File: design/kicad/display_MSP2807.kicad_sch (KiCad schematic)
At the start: 3 parts

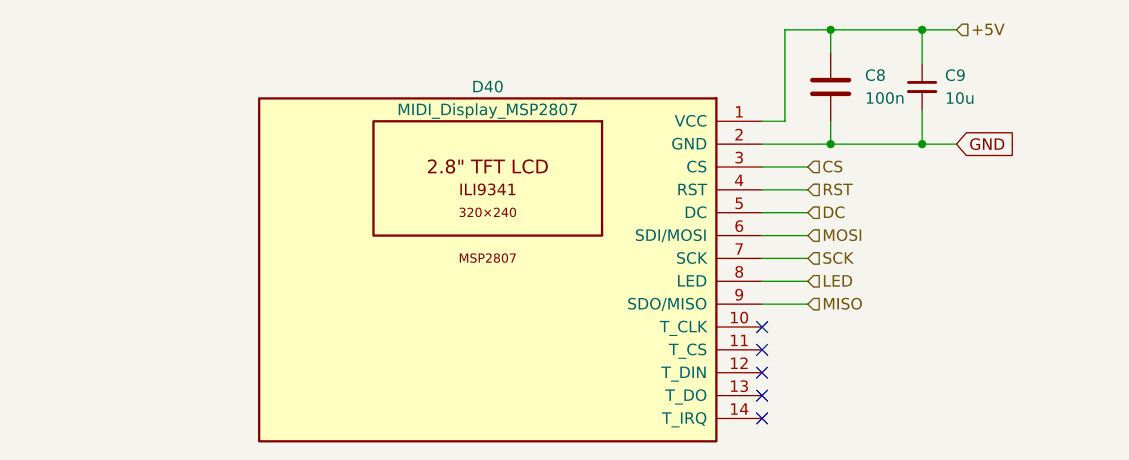
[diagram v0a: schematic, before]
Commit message: Fix reference labels and update wire connections in MIDI controller and multiplexer schematics
- Adjusted wire connection points in the MIDI controller schematic for better alignment.
- Updated label positions for various components in the MIDI controller schematic.
- Renamed reference designators for capacitors and power connections in the multiplexer schematic to maintain consistency.
- Corrected the reference designators for multiple components to reflect accurate labeling.
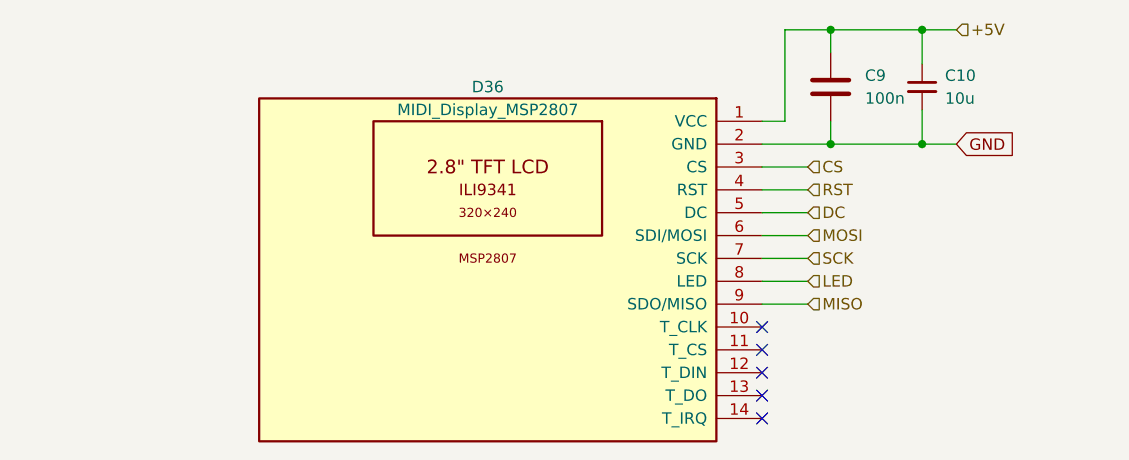
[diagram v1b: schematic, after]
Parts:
- renumbered C9 to C10, C8 to C9, D40 to D36
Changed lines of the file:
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@@
 		(dnp no)
 		(fields_autoplaced yes)
-		(property "Reference" "C9"
+		(property "Reference" "C10"
 			(at 172.72 67.3162 0)
 			(effects
@@
 			(project ""
 				(path "/9e44e663-00d0-4f33-bf1f-c4ad78deb554/b074c366-2f0b-4fcc-8b9f-7590ca8943b4"
-					(reference "C9")
+					(reference "C10")
 					(unit 1)
 				)
@@
 		(on_board yes)
 		(dnp no)
-		(property "Reference" "D40"
+		(property "Reference" "D36"
 			(at 121.92 68.58 0)
 			(effects
@@
 			(project "midi_controller"
 				(path "/9e44e663-00d0-4f33-bf1f-c4ad78deb554/b074c366-2f0b-4fcc-8b9f-7590ca8943b4"
-					(reference "D40")
+					(reference "D36")
 					(unit 1)
 				)
@@
 		(dnp no)
 		(fields_autoplaced yes)
-		(property "Reference" "C8"
+		(property "Reference" "C9"
 			(at 163.83 67.3099 0)
 			(effects
@@
 			(project "midi_controller"
 				(path "/9e44e663-00d0-4f33-bf1f-c4ad78deb554/b074c366-2f0b-4fcc-8b9f-7590ca8943b4"
-					(reference "C8")
+					(reference "C9")
 					(unit 1)
 				)

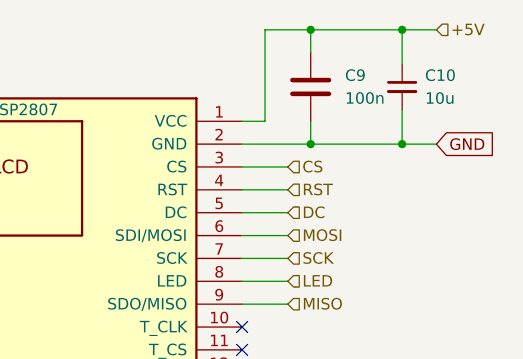
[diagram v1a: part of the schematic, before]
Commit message: Update capacitor references in multiplexer schematic
Changed capacitor references from C11 to C42 and C12 to C43 in the multiplexer_CD74HC4067M schematic. Updated instances accordingly to maintain consistency in the design.
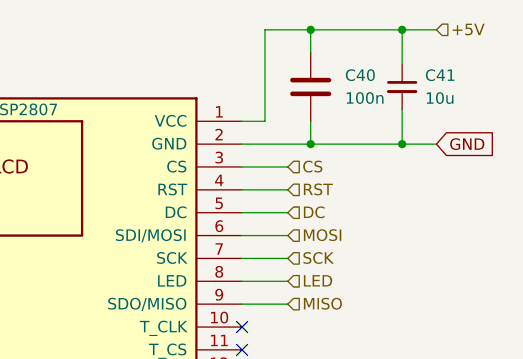
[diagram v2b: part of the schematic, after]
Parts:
- renumbered C9 to C40, C10 to C41
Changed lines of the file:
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@@
 		(dnp no)
 		(fields_autoplaced yes)
-		(property "Reference" "C10"
+		(property "Reference" "C41"
 			(at 172.72 67.3162 0)
 			(effects
@@
 			(project ""
 				(path "/9e44e663-00d0-4f33-bf1f-c4ad78deb554/b074c366-2f0b-4fcc-8b9f-7590ca8943b4"
-					(reference "C10")
+					(reference "C41")
 					(unit 1)
 				)
@@
 		(dnp no)
 		(fields_autoplaced yes)
-		(property "Reference" "C9"
+		(property "Reference" "C40"
 			(at 163.83 67.3099 0)
 			(effects
@@
 			(project "midi_controller"
 				(path "/9e44e663-00d0-4f33-bf1f-c4ad78deb554/b074c366-2f0b-4fcc-8b9f-7590ca8943b4"
-					(reference "C9")
+					(reference "C40")
 					(unit 1)
 				)

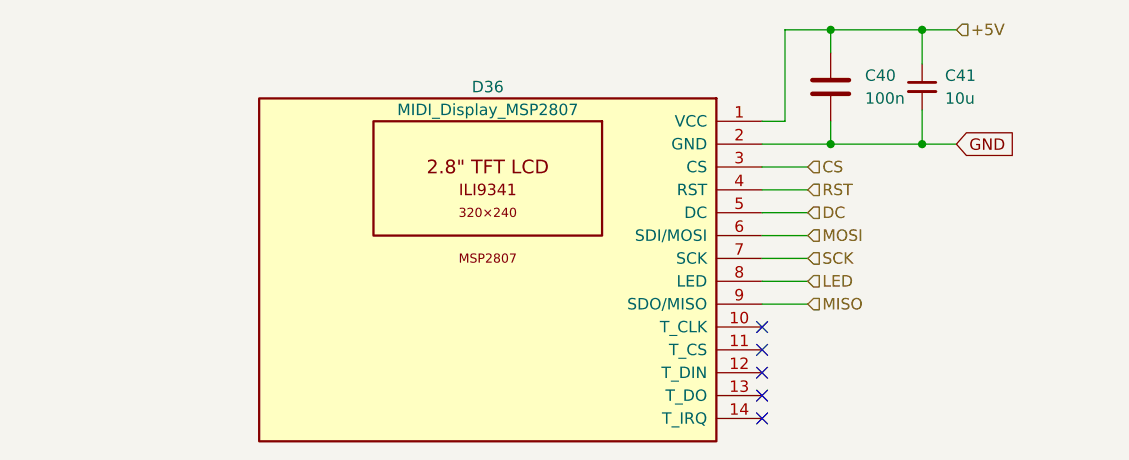
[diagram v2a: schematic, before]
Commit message: Update kicad binary files
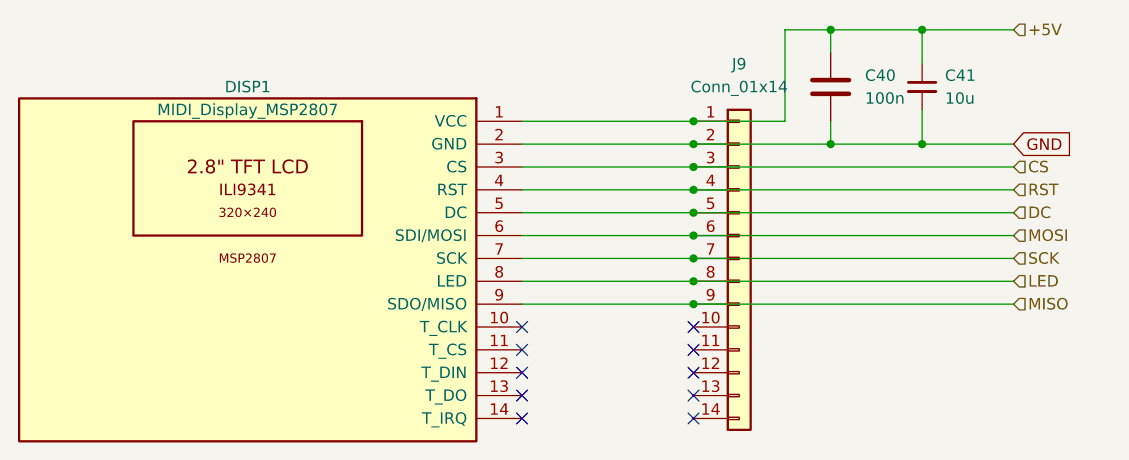
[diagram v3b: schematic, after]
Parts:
- added J9: Conn_01x14, Connector_PinSocket_2.54mm:PinSocket_1x14_P2.54mm_Vertical, symbol Connector_Generic:Conn_01x14
- renumbered D36 to DISP1
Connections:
- net +5V: now also J9.1 (Pin_1)
- net CS: now also J9.3 (Pin_3)
- net DC: now also J9.5 (Pin_5)
- net GND: now also J9.2 (Pin_2)
- net LED: now also J9.8 (Pin_8)
- net MISO: now also J9.9 (Pin_9)
- net MOSI: now also J9.6 (Pin_6)
- net RST: now also J9.4 (Pin_4)
- net SCK: now also J9.7 (Pin_7)
- no-connect marks 5 -> 10
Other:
- moved on the sheet: DISP1

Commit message: Update kicad binary files
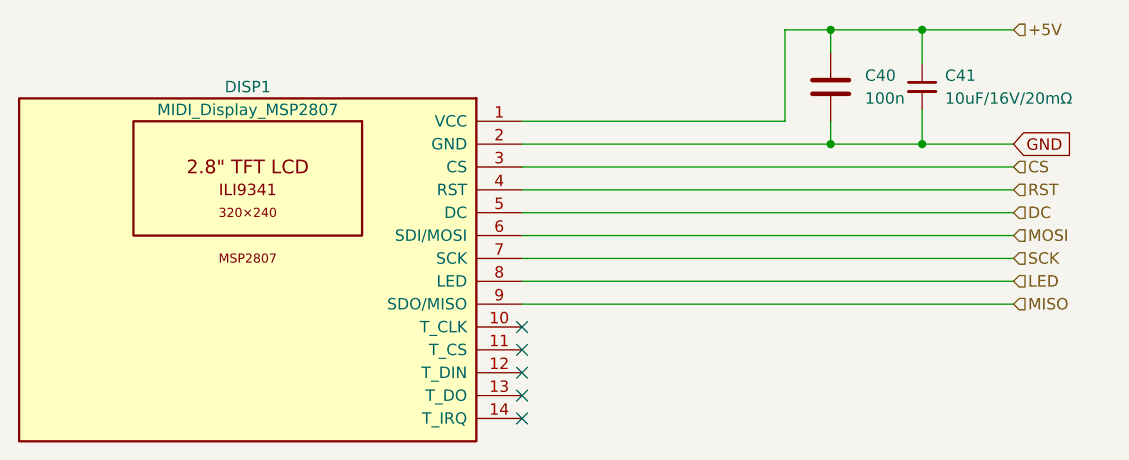
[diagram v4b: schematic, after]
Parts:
- removed J9: Conn_01x14, Connector_PinSocket_2.54mm:PinSocket_1x14_P2.54mm_Vertical, symbol Connector_Generic:Conn_01x14
- C41: footprint Capacitor_SMD:C_0805_2012Metric -> 4ms_Capacitor:C_0805; Display 10u -> 10uF/16V/20mΩ
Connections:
- no-connect marks 10 -> 5

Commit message: Update kicad binary files
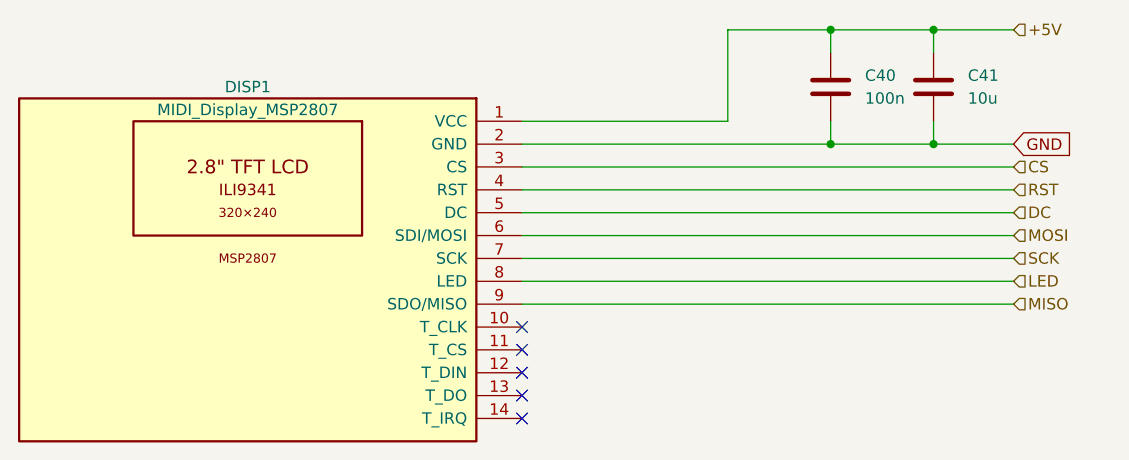
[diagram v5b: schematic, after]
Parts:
- C41: value 10uF_0805_16V_lowESR -> 10u; footprint 4ms_Capacitor:C_0805 -> Capacitor_SMD:C_0805_2012Metric; symbol PCM_4ms_Capacitor:10uF_0805_16V_lowESR -> Device:C; Display 10uF/16V/20mΩ -> (none); JLCPCB ID C190442 -> (none); Manufacturer Taiyo Yuden -> (none); Part Number EMK212ABJ106KG-T -> (none); Specifications 10uF, Min. 16V, ESR<=20mΩ@1MHz, 0805, MLCC -> (none)
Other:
- moved on the sheet: C41
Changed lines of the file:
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@@
 	(paper "A4")
+	(junction
+		(at 171.45 62.23)
+		(diameter 0)
+		(color 0 0 0 0)
+	)
 	(junction
 		(at 160.02 62.23)
@@
 	)
 	(junction
-		(at 170.18 62.23)
-		(diameter 0)
-		(color 0 0 0 0)
-	)
-	(junction
-		(at 170.18 74.93)
+		(at 171.45 74.93)
 		(diameter 0)
 		(color 0 0 0 0)
@@
 	(wire
 		(pts
-			(xy 160.02 74.93) (xy 170.18 74.93)
+			(xy 160.02 74.93) (xy 171.45 74.93)
+		)
+		(stroke
+			(width 0)
+			(type default)
+		)
+	)
+	(wire
+		(pts
+			(xy 171.45 62.23) (xy 180.34 62.23)
 		)
 		(stroke
@@
 	(wire
 		(pts
-			(xy 160.02 62.23) (xy 170.18 62.23)
-		)
-		(stroke
-			(width 0)
-			(type default)
-		)
-	)
-	(wire
-		(pts
 			(xy 125.73 82.55) (xy 180.34 82.55)
 		)
@@
 	(wire
 		(pts
+			(xy 171.45 74.93) (xy 180.34 74.93)
+		)
+		(stroke
+			(width 0)
+			(type default)
+		)
+	)
+	(wire
+		(pts
 			(xy 125.73 92.71) (xy 180.34 92.71)
 		)
@@
 	(wire
 		(pts
-			(xy 125.73 72.39) (xy 154.94 72.39)
-		)
-		(stroke
-			(width 0)
-			(type default)
-		)
-	)
-	(wire
-		(pts
-			(xy 170.18 62.23) (xy 170.18 66.04)
+			(xy 125.73 72.39) (xy 148.59 72.39)
 		)
 		(stroke
@@
 	(wire
 		(pts
-			(xy 170.18 74.93) (xy 180.34 74.93)
-		)
-		(stroke
-			(width 0)
-			(type default)
-		)
-	)
-	(wire
-		(pts
 			(xy 125.73 80.01) (xy 180.34 80.01)
 		)
@@
 	(wire
 		(pts
+			(xy 171.45 62.23) (xy 171.45 64.77)
+		)
+		(stroke
+			(width 0)
+			(type default)
+		)
+	)
+	(wire
+		(pts
 			(xy 160.02 72.39) (xy 160.02 74.93)
 		)
@@
 	(wire
 		(pts
-			(xy 170.18 62.23) (xy 180.34 62.23)
+			(xy 160.02 62.23) (xy 171.45 62.23)
 		)
 		(stroke
@@
 	(wire
 		(pts
-			(xy 154.94 62.23) (xy 160.02 62.23)
-		)
-		(stroke
-			(width 0)
-			(type default)
-		)
-	)
-	(wire
-		(pts
-			(xy 154.94 62.23) (xy 154.94 72.39)
-		)
-		(stroke
-			(width 0)
-			(type default)
-		)
-	)
-	(wire
-		(pts
-			(xy 170.18 71.12) (xy 170.18 74.93)
+			(xy 148.59 62.23) (xy 160.02 62.23)
+		)
+		(stroke
+			(width 0)
+			(type default)
+		)
+	)
+	(wire
+		(pts
+			(xy 171.45 72.39) (xy 171.45 74.93)
+		)
+		(stroke
+			(width 0)
+			(type default)
+		)
+	)
+	(wire
+		(pts
+			(xy 148.59 62.23) (xy 148.59 72.39)
 		)
 		(stroke
@@
 	)
 	(symbol
-		(lib_id "PCM_4ms_Capacitor:10uF_0805_16V_lowESR")
-		(at 170.18 68.58 0)
+		(lib_id "Device:C")
+		(at 171.45 68.58 0)
 		(unit 1)
 		(exclude_from_sim no)
@@
 		(fields_autoplaced yes)
 		(property "Reference" "C41"
-			(at 172.72 67.3162 0)
+			(at 175.26 67.3099 0)
 			(effects
 				(font
@@
 			)
 		)
-		(property "Value" "10uF_0805_16V_lowESR"
-			(at 170.18 64.77 0)
+		(property "Value" "10u"
+			(at 175.26 69.8499 0)
+			(effects
+				(font
+					(size 1.27 1.27)
+				)
+				(justify left)
+			)
+		)
+		(property "Footprint" "Capacitor_SMD:C_0805_2012Metric"
+			(at 172.4152 72.39 0)
 			(effects
 				(font
@@
 			)
 		)
-		(property "Footprint" "4ms_Capacitor:C_0805"
-			(at 167.64 73.66 0)
-			(effects
-				(font
-					(size 1.27 1.27)
-				)
-				(justify left)
+		(property "Datasheet" "~"
+			(at 171.45 68.58 0)
+			(effects
+				(font
+					(size 1.27 1.27)
+				)
 				(hide yes)
 			)
 		)
-		(property "Datasheet" ""
-			(at 170.18 68.58 0)
-			(effects
-				(font
-					(size 1.27 1.27)
-				)
-				(hide yes)
-			)
-		)
-		(property "Description" "10uF, Min. 16V, ESR<=20mΩ@1MHz, 0805, MLCC"
-			(at 170.18 68.58 0)
-			(effects
-				(font
-					(size 1.27 1.27)
-				)
-				(hide yes)
-			)
-		)
-		(property "Specifications" "10uF, Min. 16V, ESR<=20mΩ@1MHz, 0805, MLCC"
-			(at 167.64 76.454 0)
-			(effects
-				(font
-					(size 1.27 1.27)
-				)
-				(justify left)
-				(hide yes)
-			)
-		)
-		(property "Manufacturer" "Taiyo Yuden"
-			(at 167.64 77.978 0)
-			(effects
-				(font
-					(size 1.27 1.27)
-				)
-				(justify left)
-				(hide yes)
-			)
-		)
-		(property "Part Number" "EMK212ABJ106KG-T"
-			(at 167.64 79.502 0)
-			(effects
-				(font
-					(size 1.27 1.27)
-				)
-				(justify left)
-				(hide yes)
-			)
-		)
-		(property "Display" "10uF/16V/20mΩ"
-			(at 172.72 69.8562 0)
-			(effects
-				(font
-					(size 1.27 1.27)
-				)
-				(justify left)
-			)
-		)
-		(property "JLCPCB ID" "C190442"
-			(at 170.18 68.58 0)
-			(effects
-				(font
+		(property "Description" "Unpolarized capacitor"
+			(at 171.45 68.58 0)
+			(effects
+				(font

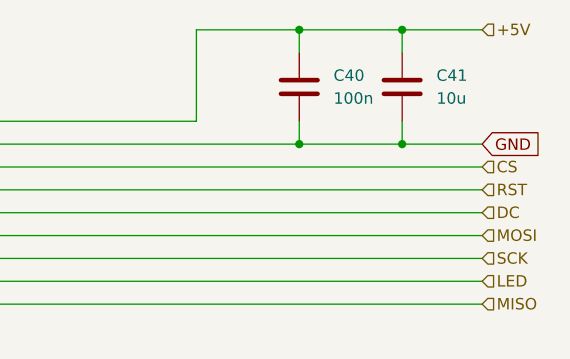
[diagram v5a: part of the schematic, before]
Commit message: Update kicad binary files
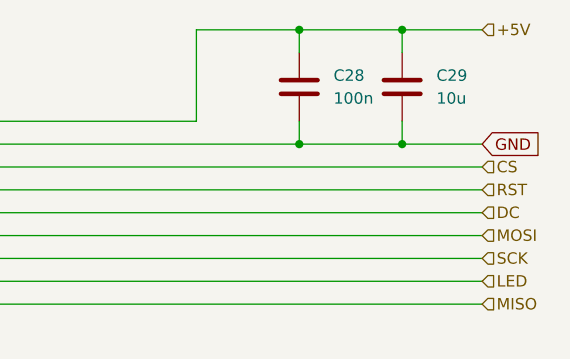
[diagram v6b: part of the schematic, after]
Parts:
- C28: renamed from C40; LCSC (none) -> C1711
- C29: renamed from C41; Display (none) -> 10u; JLCPCB ID (none) -> C1713; LCSC (none) -> C1713; Manufacturer (none) -> Taiyo Yuden; Part Number (none) -> EMK212ABJ106KG-T; Specifications (none) -> 10uF, Min. 16V, ESR<=20mΩ@1MHz, 0805, MLCC
- DISP1: now left out of the parts list
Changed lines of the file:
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@@
 		(dnp no)
 		(fields_autoplaced yes)
-		(property "Reference" "C41"
+		(property "Reference" "C29"
 			(at 175.26 67.3099 0)
 			(effects
@@
 		)
 		(property "Description" "Unpolarized capacitor"
+			(at 171.45 68.58 0)
+			(effects
+				(font
+					(size 1.27 1.27)
+				)
+				(hide yes)
+			)
+		)
+		(property "LCSC" "C1713"
+			(at 175.26 67.3099 0)
+			(effects
+				(font
+					(size 1.27 1.27)
+				)
+				(hide yes)
+			)
+		)
+		(property "Display" "10u"
+			(at 171.45 68.58 0)
+			(effects
+				(font
+					(size 1.27 1.27)
+				)
+				(hide yes)
+			)
+		)
+		(property "JLCPCB ID" "C1713"
+			(at 171.45 68.58 0)
+			(effects
+				(font
+					(size 1.27 1.27)
+				)
+				(hide yes)
+			)
+		)
+		(property "Manufacturer" "Taiyo Yuden"
+			(at 171.45 68.58 0)
+			(effects
+				(font
+					(size 1.27 1.27)
+				)
+				(hide yes)
+			)
+		)
+		(property "Part Number" "EMK212ABJ106KG-T"
+			(at 171.45 68.58 0)
+			(effects
+				(font
+					(size 1.27 1.27)
+				)
+				(hide yes)
+			)
+		)
+		(property "Specifications" "10uF, Min. 16V, ESR<=20mΩ@1MHz, 0805, MLCC"
 			(at 171.45 68.58 0)
 			(effects
@@
 			(project ""
 				(path "/9e44e663-00d0-4f33-bf1f-c4ad78deb554/b074c366-2f0b-4fcc-8b9f-7590ca8943b4"
-					(reference "C41")
+					(reference "C29")
 					(unit 1)
 				)
@@
 		(unit 1)
 		(exclude_from_sim no)
-		(in_bom yes)
+		(in_bom no)
 		(on_board yes)
 		(dnp no)
@@
 		(dnp no)
 		(fields_autoplaced yes)
-		(property "Reference" "C40"
+		(property "Reference" "C28"
 			(at 163.83 67.3099 0)
 			(effects
@@
 		(property "Description" "Unpolarized capacitor"
 			(at 160.02 68.58 0)
+			(effects
+				(font
+					(size 1.27 1.27)
+				)
+				(hide yes)
+			)
+		)
+		(property "LCSC" "C1711"
+			(at 163.83 67.3099 0)
 			(effects
 				(font
@@
 			(project "midi_controller"
 				(path "/9e44e663-00d0-4f33-bf1f-c4ad78deb554/b074c366-2f0b-4fcc-8b9f-7590ca8943b4"
-					(reference "C40")
+					(reference "C28")
 					(unit 1)
 				)

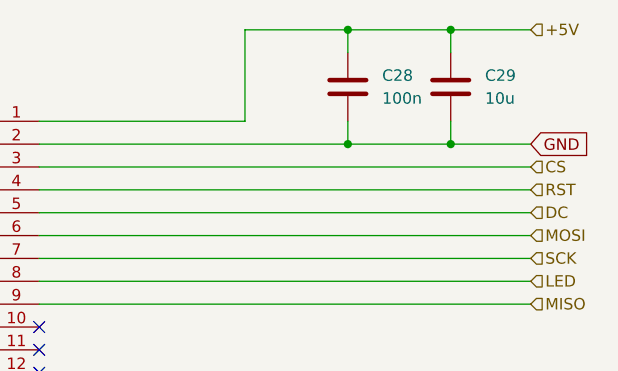
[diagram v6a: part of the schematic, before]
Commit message: Update kicad binary files
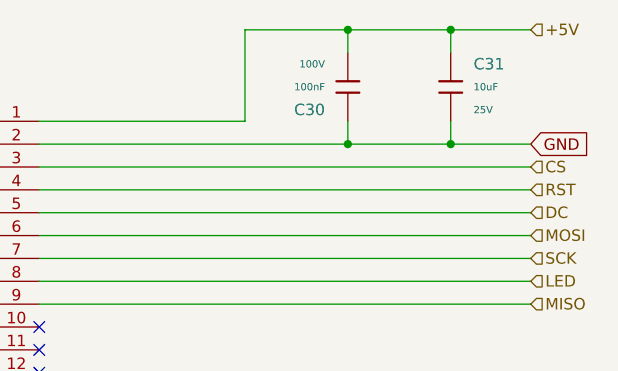
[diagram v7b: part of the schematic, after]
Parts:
- removed C28: 100n, Capacitor_SMD:C_0805_2012Metric, symbol Device:C
- removed C29: 10u, Capacitor_SMD:C_0805_2012Metric, symbol Device:C
- added C30: 100nF, PCM_JLCPCB:C_0805, symbol PCM_JLCPCB-Capacitors:0805,100nF
- added C31: 10uF, PCM_JLCPCB:C_0805, symbol PCM_JLCPCB-Capacitors:0805,10uF
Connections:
- net +5V: now also C30.2, C31.1
- net GND: now also C30.1, C31.2
